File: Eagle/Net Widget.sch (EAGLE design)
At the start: 19 parts, among them IC1 ATmega1284P

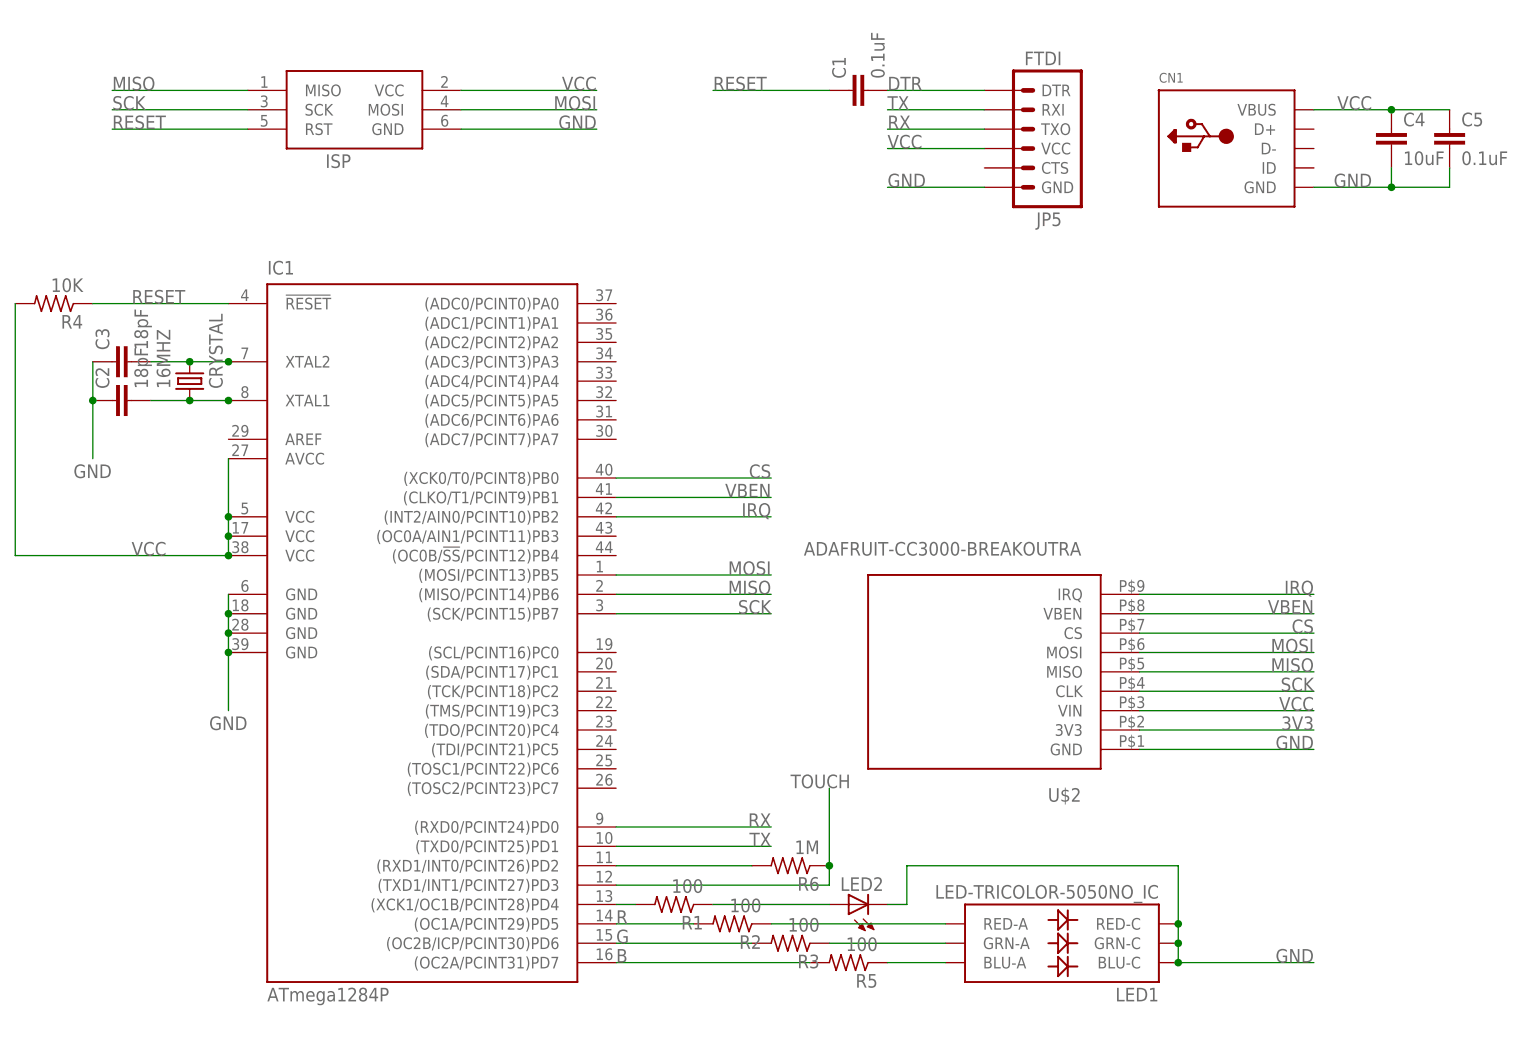
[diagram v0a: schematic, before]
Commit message: Re-arrange LEDs and touch point.
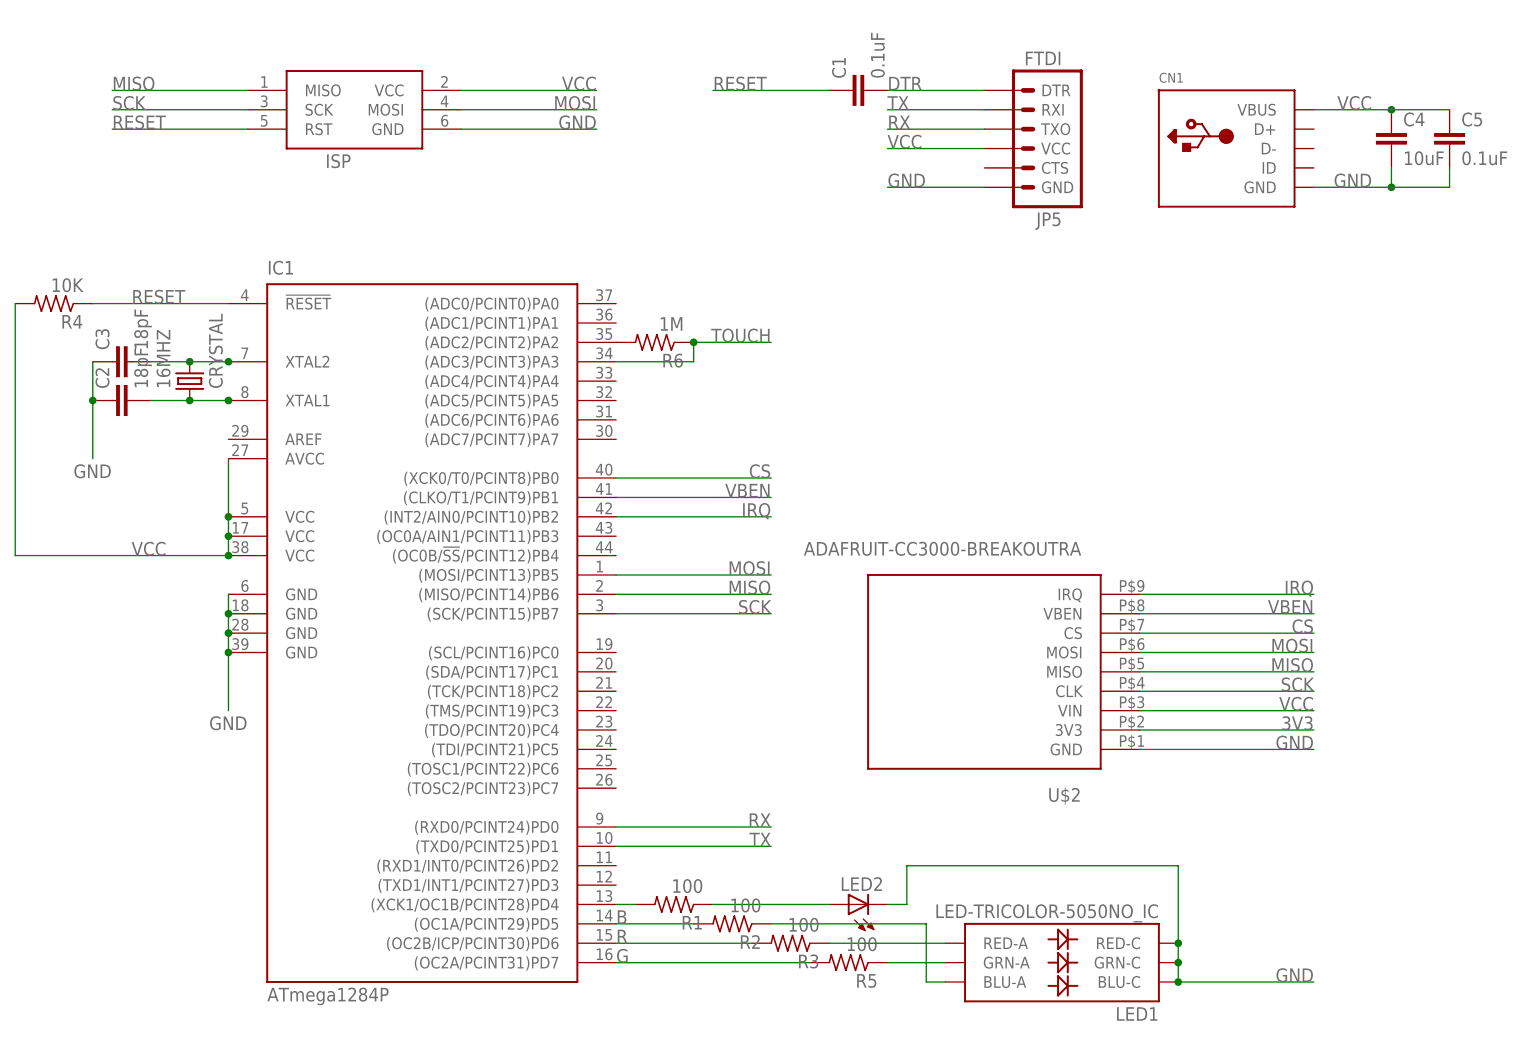
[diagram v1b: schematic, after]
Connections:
- removed net N$10: LED1.RED-A, R2.1
- removed net N$11: LED1.GRN-A, R3.1
- removed net N$12: LED1.BLU-A, R5.1
- new net N$2: LED1.RED-A, R3.1
- new net N$4: LED1.GRN-A, R5.1
- new net N$5: LED1.BLU-A, R2.1
- net B: now also IC1.(OC1A/PCINT29)PD5, R2.2; no longer IC1.(OC2A/PCINT31)PD7, R5.2
- net G: now also IC1.(OC2A/PCINT31)PD7, R5.2; no longer IC1.(OC2B/ICP/PCINT30)PD6, R3.2
- net N$1: now also IC1.(ADC2/PCINT2)PA2; no longer IC1.(RXD1/INT0/PCINT26)PD2
- net R: now also IC1.(OC2B/ICP/PCINT30)PD6, R3.2; no longer IC1.(OC1A/PCINT29)PD5, R2.2
- net TOUCH: now also IC1.(ADC3/PCINT3)PA3; no longer IC1.(TXD1/INT1/PCINT27)PD3
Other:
- moved on the sheet: LED1, R6
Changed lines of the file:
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@@
 <instance part="C1" gate="G$1" x="114.3" y="109.22" rot="R90"/>
 <instance part="CN1" gate="G$1" x="165.1" y="101.6"/>
-<instance part="LED1" gate="D1" x="142.24" y="-2.54" rot="R180"/>
+<instance part="LED1" gate="D1" x="142.24" y="-5.08" rot="R180"/>
 <instance part="LED2" gate="G$1" x="114.3" y="2.54" rot="R90"/>
 <instance part="R1" gate="G$1" x="91.44" y="2.54" rot="R180"/>
@@
 <instance part="R3" gate="G$1" x="106.68" y="-2.54" rot="R180"/>
 <instance part="R5" gate="G$1" x="114.3" y="-5.08" rot="R180"/>
-<instance part="R6" gate="G$1" x="106.68" y="7.62" rot="R180"/>
+<instance part="R6" gate="G$1" x="88.9" y="76.2" rot="R180"/>
 </instances>
 <busses>
@@
 <pinref part="LED1" gate="D1" pin="BLU-C"/>
 <pinref part="LED1" gate="D1" pin="GRN-C"/>
+<wire x1="157.48" y1="-7.62" x2="157.48" y2="-5.08" width="0.1524" layer="91"/>
+<pinref part="LED1" gate="D1" pin="RED-C"/>
 <wire x1="157.48" y1="-5.08" x2="157.48" y2="-2.54" width="0.1524" layer="91"/>
-<pinref part="LED1" gate="D1" pin="RED-C"/>
-<wire x1="157.48" y1="-2.54" x2="157.48" y2="0" width="0.1524" layer="91"/>
+<junction x="157.48" y="-5.08"/>
 <junction x="157.48" y="-2.54"/>
-<junction x="157.48" y="0"/>
-<label x="175.26" y="-5.08" size="1.778" layer="95" rot="MR0"/>
-<wire x1="157.48" y1="-5.08" x2="175.26" y2="-5.08" width="0.1524" layer="91"/>
-<junction x="157.48" y="-5.08"/>
+<label x="175.26" y="-7.62" size="1.778" layer="95" rot="MR0"/>
+<wire x1="157.48" y1="-7.62" x2="175.26" y2="-7.62" width="0.1524" layer="91"/>
+<junction x="157.48" y="-7.62"/>
 <pinref part="LED2" gate="G$1" pin="C"/>
 <wire x1="119.38" y1="2.54" x2="121.92" y2="2.54" width="0.1524" layer="91"/>
 <wire x1="121.92" y1="2.54" x2="121.92" y2="7.62" width="0.1524" layer="91"/>
 <wire x1="121.92" y1="7.62" x2="157.48" y2="7.62" width="0.1524" layer="91"/>
-<wire x1="157.48" y1="7.62" x2="157.48" y2="0" width="0.1524" layer="91"/>
+<wire x1="157.48" y1="7.62" x2="157.48" y2="-2.54" width="0.1524" layer="91"/>
 </segment>
 </net>
@@
 </segment>
 </net>
-<net name="R" class="0">
+<net name="B" class="0">
 <segment>
 <pinref part="IC1" gate="G$1" pin="(OC1A/PCINT29)PD5"/>
@@
 </segment>
 </net>
-<net name="G" class="0">
+<net name="R" class="0">
 <segment>
 <pinref part="IC1" gate="G$1" pin="(OC2B/ICP/PCINT30)PD6"/>
@@
 </segment>
 </net>
-<net name="B" class="0">
+<net name="G" class="0">
 <segment>
 <pinref part="IC1" gate="G$1" pin="(OC2A/PCINT31)PD7"/>
@@
 </segment>
 </net>
-<net name="N$10" class="0">
+<net name="TOUCH" class="0">
+<segment>
+<pinref part="R6" gate="G$1" pin="1"/>
+<wire x1="93.98" y1="76.2" x2="104.14" y2="76.2" width="0.1524" layer="91"/>
+<label x="104.14" y="76.2" size="1.778" layer="95" rot="MR0"/>
+<pinref part="IC1" gate="G$1" pin="(ADC3/PCINT3)PA3"/>
+<wire x1="83.82" y1="73.66" x2="93.98" y2="73.66" width="0.1524" layer="91"/>
+<wire x1="93.98" y1="73.66" x2="93.98" y2="76.2" width="0.1524" layer="91"/>
+<junction x="93.98" y="76.2"/>
+</segment>
+</net>
+<net name="N$1" class="0">
+<segment>
+<pinref part="IC1" gate="G$1" pin="(ADC2/PCINT2)PA2"/>
+<pinref part="R6" gate="G$1" pin="2"/>
+</segment>
+</net>
+<net name="N$2" class="0">
+<segment>
+<pinref part="R3" gate="G$1" pin="1"/>
+<pinref part="LED1" gate="D1" pin="RED-A"/>
+<wire x1="111.76" y1="-2.54" x2="127" y2="-2.54" width="0.1524" layer="91"/>
+</segment>
+</net>
+<net name="N$4" class="0">
+<segment>
+<pinref part="R5" gate="G$1" pin="1"/>
+<pinref part="LED1" gate="D1" pin="GRN-A"/>
+<wire x1="119.38" y1="-5.08" x2="127" y2="-5.08" width="0.1524" layer="91"/>
+</segment>
+</net>
+<net name="N$5" class="0">
 <segment>
 <pinref part="R2" gate="G$1" pin="1"/>
-<pinref part="LED1" gate="D1" pin="RED-A"/>
-<wire x1="127" y1="0" x2="104.14" y2="0" width="0.1524" layer="91"/>
-</segment>
-</net>
-<net name="N$11" class="0">
-<segment>
-<pinref part="R3" gate="G$1" pin="1"/>
-<pinref part="LED1" gate="D1" pin="GRN-A"/>
-<wire x1="127" y1="-2.54" x2="111.76" y2="-2.54" width="0.1524" layer="91"/>
-</segment>
-</net>
-<net name="N$12" class="0">
-<segment>
-<pinref part="R5" gate="G$1" pin="1"/>
+<wire x1="104.14" y1="0" x2="124.46" y2="0" width="0.1524" layer="91"/>
+<wire x1="124.46" y1="0" x2="124.46" y2="-7.62" width="0.1524" layer="91"/>
 <pinref part="LED1" gate="D1" pin="BLU-A"/>
-<wire x1="127" y1="-5.08" x2="119.38" y2="-5.08" width="0.1524" layer="91"/>
-</segment>
-</net>
-<net name="N$1" class="0">
-<segment>
-<pinref part="IC1" gate="G$1" pin="(RXD1/INT0/PCINT26)PD2"/>
-<pinref part="R6" gate="G$1" pin="2"/>
-<wire x1="101.6" y1="7.62" x2="83.82" y2="7.62" width="0.1524" layer="91"/>
-</segment>
-</net>
-<net name="TOUCH" class="0">
-<segment>
-<pinref part="IC1" gate="G$1" pin="(TXD1/INT1/PCINT27)PD3"/>
-<pinref part="R6" gate="G$1" pin="1"/>
-<wire x1="83.82" y1="5.08" x2="111.76" y2="5.08" width="0.1524" layer="91"/>
-<wire x1="111.76" y1="5.08" x2="111.76" y2="7.62" width="0.1524" layer="91"/>
-<wire x1="111.76" y1="7.62" x2="111.76" y2="17.78" width="0.1524" layer="91"/>
-<junction x="111.76" y="7.62"/>
-<label x="106.68" y="17.78" size="1.778" layer="95"/>
-</segment>
-</net>
+<wire x1="124.46" y1="-7.62" x2="127" y2="-7.62" width="0.1524" layer="91"/>
+</segment>
+</net>

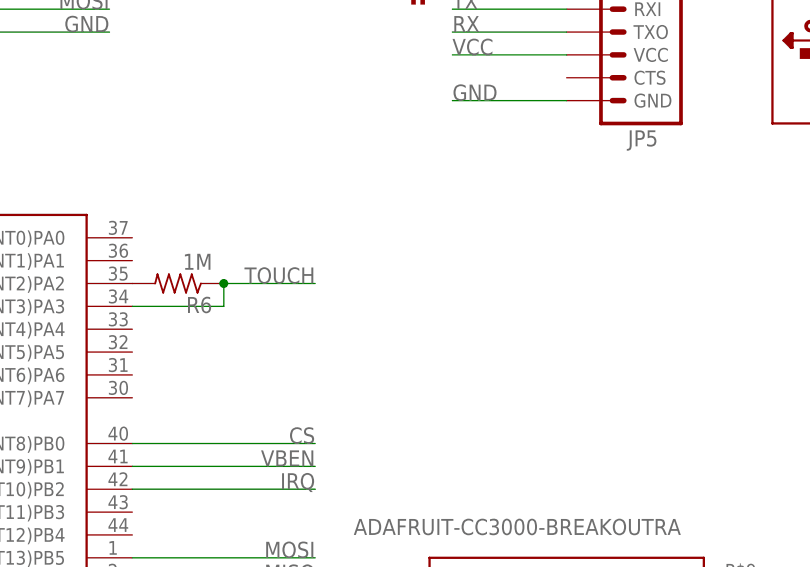
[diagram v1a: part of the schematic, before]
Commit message: Add alligator clip connector and adjust silkscreen
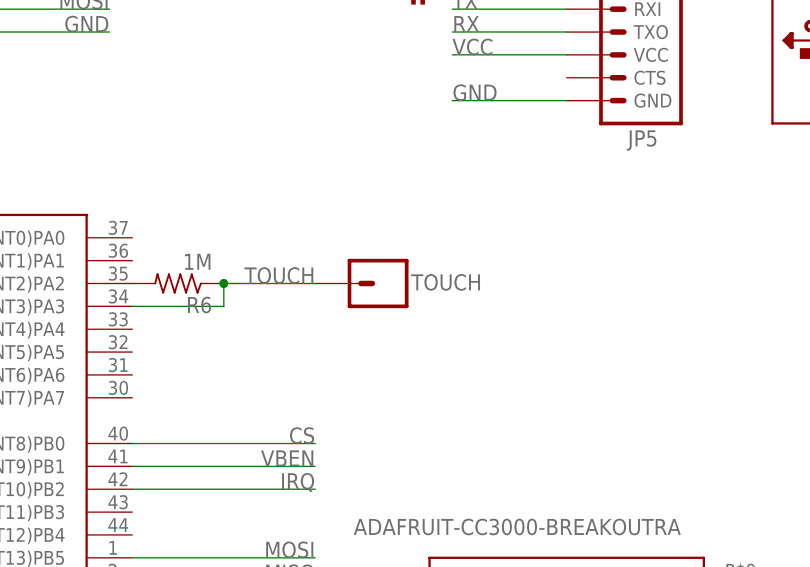
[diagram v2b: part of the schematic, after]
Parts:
- added TOUCH: M01ALLIGATOR-3MM, SparkFun-Connectors:M01ALLIGATOR-3MM
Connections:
- net TOUCH: now also TOUCH.1
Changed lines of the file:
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@@
 <part name="R5" library="rcl" deviceset="R-US_" device="R1206" value="100"/>
 <part name="R6" library="rcl" deviceset="R-US_" device="R1206" value="1M"/>
+<part name="TOUCH" library="SparkFun-Connectors" deviceset="M01" device="ALLIGATOR-3MM" value=""/>
 </parts>
 <sheets>
@@
 <instance part="R5" gate="G$1" x="114.3" y="-5.08" rot="R180"/>
 <instance part="R6" gate="G$1" x="88.9" y="76.2" rot="R180"/>
+<instance part="TOUCH" gate="G$1" x="111.76" y="76.2" smashed="yes" rot="MR0">
+<attribute name="VALUE" x="114.3" y="71.12" size="1.778" layer="96" rot="MR0"/>
+<attribute name="NAME" x="114.808" y="77.216" size="1.778" layer="95" rot="MR180"/>
+</instance>
 </instances>
 <busses>
@@
 <wire x1="93.98" y1="73.66" x2="93.98" y2="76.2" width="0.1524" layer="91"/>
 <junction x="93.98" y="76.2"/>
-</segment>
-</net>
+<pinref part="TOUCH" gate="G$1" pin="1"/>
+</segment>
+</net>
